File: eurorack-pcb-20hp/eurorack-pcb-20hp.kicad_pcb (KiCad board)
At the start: 2 copper layers, 49 x 108.3 mm, 0 parts

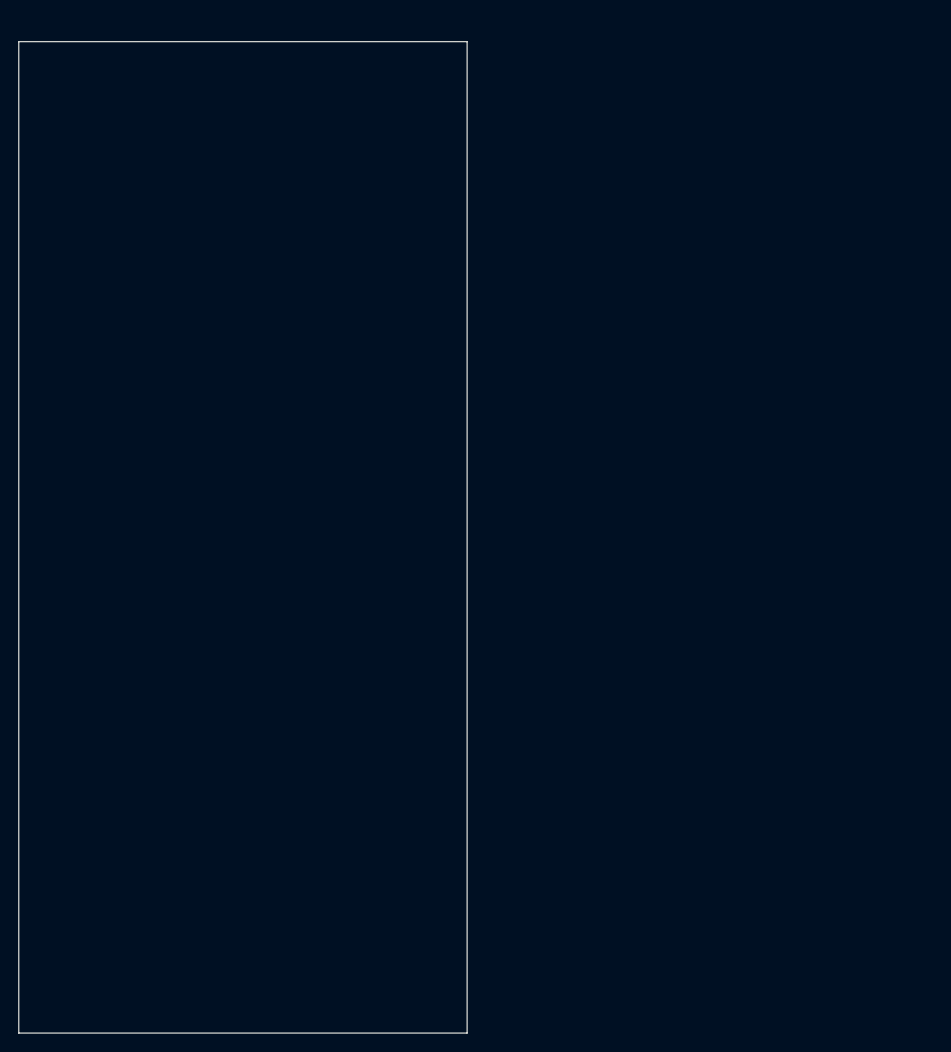
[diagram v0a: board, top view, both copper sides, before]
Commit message: Minor adjustments to PCB positioning. Moving everything into a single folder to be easier for kiCad to pick up all templates from user-template path
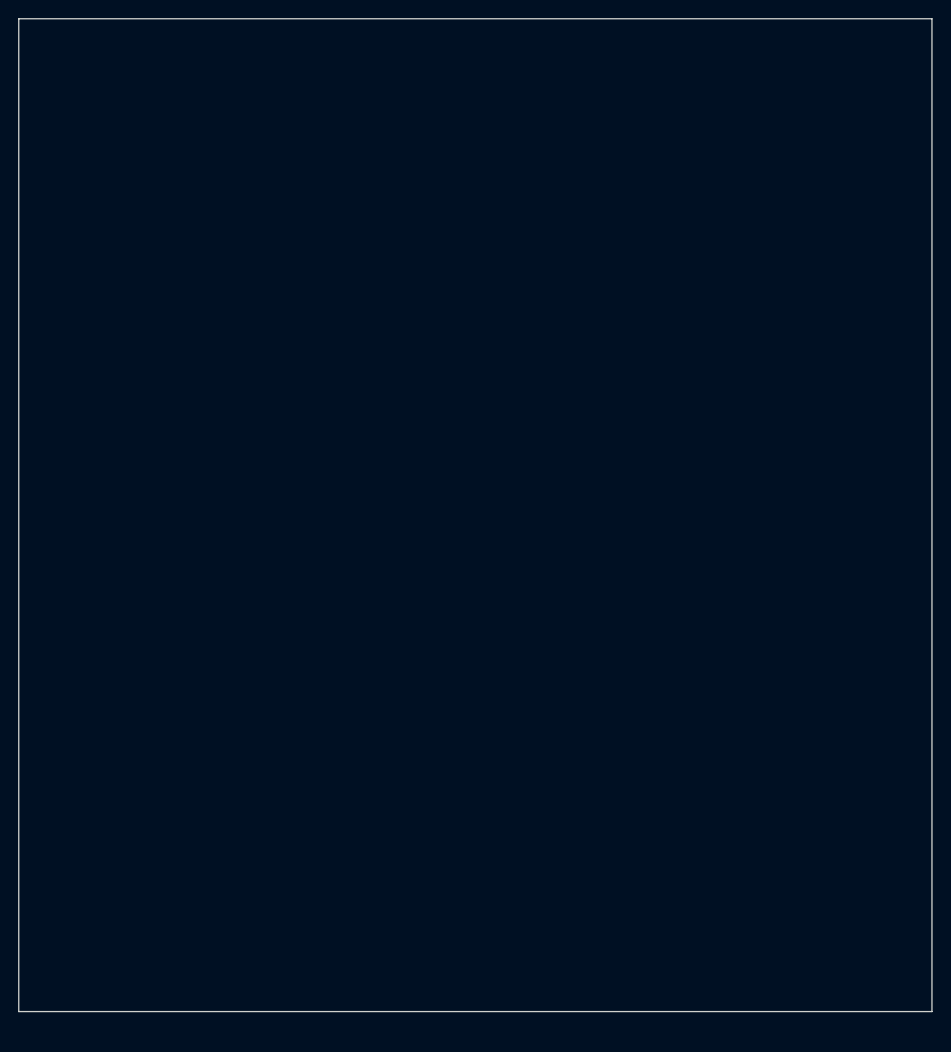
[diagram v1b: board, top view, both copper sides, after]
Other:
- board size 49 x 108.3 mm -> 99.8 x 108.5 mm
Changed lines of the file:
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@@
   )
   (net 0 "")
-  (gr_line (start 0.75 12.5) (end 0.75 120.85) (layer "Edge.Cuts") (width 0.1))
-  (gr_line (start 49.75 120.85) (end 49.75 12.5) (layer "Edge.Cuts") (width 0.1))
-  (gr_line (start 0.75 120.85) (end 49.75 120.85) (layer "Edge.Cuts") (width 0.1))
-  (gr_line (start 0.75 12.5) (end 49.75 12.5) (layer "Edge.Cuts") (width 0.1))
-  (gr_line (start 50.5 0) (end 50.5 128.5) (layer "User.1") (width 0.1))
+  (gr_line (start 0.75 10) (end 0.75 118.5) (layer "Edge.Cuts") (width 0.1))
+  (gr_line (start 100.55 118.5) (end 100.55 10) (layer "Edge.Cuts") (width 0.1))
+  (gr_line (start 0.75 118.5) (end 100.55 118.5) (layer "Edge.Cuts") (width 0.1))
+  (gr_line (start 0.75 10) (end 100.55 10) (layer "Edge.Cuts") (width 0.1))
+  (gr_line (start 101.3 0) (end 101.3 128.5) (layer "User.1") (width 0.1))
   (gr_line (start 0 128.5) (end 0 0) (layer "User.1") (width 0.1))
-  (gr_line (start 0 0) (end 50.5 0) (layer "User.1") (width 0.1))
-  (gr_line (start 50.5 128.5) (end 0 128.5) (layer "User.1") (width 0.1))
+  (gr_line (start 0 0) (end 101.3 0) (layer "User.1") (width 0.1))
+  (gr_line (start 101.3 128.5) (end 0 128.5) (layer "User.1") (width 0.1))
 )
